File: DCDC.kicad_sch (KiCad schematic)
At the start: 58 parts, among them Q2 TCKE800NL, U16 AP3441SHE-7B, U3 AP64502QSP-13, U5 AP64502, U6 CH221K

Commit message: change cad data
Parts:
- removed C108: 100n, Capacitor_SMD:C_0402_1005Metric, symbol Device:C
- added D12: D, CM5IO:US2H_TOS, symbol Device:D
- added D13: D, CM5IO:SOD-963 CST2C_TOS, symbol Device:D
- C133: renamed from C111; value 4.7nF -> 22pF; footprint Capacitor_SMD:C_0402_1005Metric -> Capacitor_SMD:C_0603_1608Metric_Pad1.08x0.95mm_HandSolder
- C18: renamed from C4; footprint Capacitor_SMD:C_0805_2012Metric_Pad1.18x1.45mm_HandSolder -> Capacitor_SMD:C_1206_3216Metric_Pad1.33x1.80mm_HandSolder
- C19: renamed from C5; footprint Capacitor_SMD:C_0805_2012Metric_Pad1.18x1.45mm_HandSolder -> Capacitor_SMD:C_1206_3216Metric_Pad1.33x1.80mm_HandSolder
- C20: renamed from C6; footprint Capacitor_SMD:C_0805_2012Metric_Pad1.18x1.45mm_HandSolder -> Capacitor_SMD:C_1206_3216Metric_Pad1.33x1.80mm_HandSolder
- C21: renamed from C7; footprint Capacitor_SMD:C_0805_2012Metric_Pad1.18x1.45mm_HandSolder -> Capacitor_SMD:C_1206_3216Metric_Pad1.33x1.80mm_HandSolder
- C28: renamed from C14; footprint Capacitor_SMD:C_0805_2012Metric_Pad1.18x1.45mm_HandSolder -> Capacitor_SMD:C_1206_3216Metric_Pad1.33x1.80mm_HandSolder
- C29: renamed from C15; footprint Capacitor_SMD:C_0805_2012Metric_Pad1.18x1.45mm_HandSolder -> Capacitor_SMD:C_1206_3216Metric_Pad1.33x1.80mm_HandSolder
- C30: renamed from C16; footprint Capacitor_SMD:C_0805_2012Metric_Pad1.18x1.45mm_HandSolder -> Capacitor_SMD:C_1206_3216Metric_Pad1.33x1.80mm_HandSolder
- C31: renamed from C17; footprint Capacitor_SMD:C_0805_2012Metric_Pad1.18x1.45mm_HandSolder -> Capacitor_SMD:C_1206_3216Metric_Pad1.33x1.80mm_HandSolder
- C44: renamed from C30; footprint Capacitor_SMD:C_0805_2012Metric_Pad1.18x1.45mm_HandSolder -> Capacitor_SMD:C_0402_1005Metric_Pad0.74x0.62mm_HandSolder
- R65: renamed from R48; value 10K 1% -> 100kΩ; footprint Resistor_SMD:R_0402_1005Metric -> Resistor_SMD:R_0603_1608Metric_Pad0.98x0.95mm_HandSolder
- R67: renamed from R47; value 2.2K 1% -> 100kΩ; footprint Resistor_SMD:R_0402_1005Metric -> Resistor_SMD:R_0603_1608Metric_Pad0.98x0.95mm_HandSolder
- U17: renamed from U16; value AP3441SHE-7B -> AP3445LW6-7; footprint Package_DFN_QFN:DFN-8-1EP_2x2mm_P0.5mm_EP1.05x1.75mm -> Package_TO_SOT_SMD:SOT-23-6_Handsoldering
- renumbered C91 to C114, C88 to C115, C89 to C116, C90 to C117, C107 to C127, C106 to C130, C3 to C16, C8 to C22, C9 to C23, C10 to C24, C11 to C25, C13 to C27, C18 to C32, C19 to C33, C20 to C34, C21 to C35, C26 to C40, R3 to R13, R4 to R14, R5 to R15, R6 to R16, R10 to R20, R11 to R21, R12 to R22, R13 to R23, R14 to R24, R15 to R25, R16 to R26, R17 to R27, R19 to R28, R49 to R66, R50 to R68, R18 to R69, U3 to U5, U5 to U7, U6 to U8
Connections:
- net 5V: now also U17.1 (EN), U17.4 (VIN); no longer U17.3 (VIN), U17.7 (EN)
- net GND: now also U17.2 (GND), D12.2 (A), D13.2 (A); no longer U17.4 (PGND), U17.8 (SGND), U17.9 (PAD)
- net VBUS: now also D13.1 (K); no longer C23.1, C25.1, C33.1, C35.1, Q2.6 (VOUT), Q2.7 (VOUT_2), Q2.8 (VOUT_3), TP3.1, U5.2 (VIN), U5.3 (EN), U7.2 (VIN), U7.3 (EN)
- net at L4.1: now also U17.3 (LX); no longer U17.6 (LX)
- net FB: no longer names the net of C133.2, R65.2, R67.1
- net FB: now also U17.6 (FB); no longer U17.1 (FB)
- new net +12V: C23.1, C25.1, C33.1, C35.1, D12.1 (K), Q2.6 (VOUT), Q2.7 (VOUT_2), Q2.8 (VOUT_3), TP3.1, U5.2 (VIN), U5.3 (EN), U7.2 (VIN), U7.3 (EN)
- no-connect marks 2 -> 1
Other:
- note added: "1.2V DCDC"
- note added: "3.3V DCDC"
- note added: "5V DCDC"
- moved on the sheet: C114, C115, C116, C117, C127, C130, C133, C40, C44, L4, Q2, R25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

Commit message: remove efuse
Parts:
- removed C44: 1μF, Capacitor_SMD:C_0402_1005Metric_Pad0.74x0.62mm_HandSolder, symbol Device:C
- removed D12: D, CM5IO:US2H_TOS, symbol Device:D
- removed D13: D, CM5IO:SOD-963 CST2C_TOS, symbol Device:D
- removed Q2: TCKE800NL, CM5IO:TCKE800NL, symbol TCKE800NL:TCKE800NL
- removed R25: 36kΩ, Resistor_SMD:R_0603_1608Metric_Pad0.98x0.95mm_HandSolder, symbol Device:R
- removed R28: 1kΩ, Resistor_SMD:R_0603_1608Metric_Pad0.98x0.95mm_HandSolder, symbol Device:R
- removed R69: 10kΩ, Resistor_SMD:R_0603_1608Metric_Pad0.98x0.95mm_HandSolder, symbol Device:R
- removed TP3: TestPoint, TestPoint:TestPoint_Pad_2.0x2.0mm, symbol Connector:TestPoint
- renumbered C16 to C10, C114 to C103, C115 to C104, C116 to C105, C117 to C106, C127 to C114, C130 to C120, C133 to C121, C18 to C14, C19 to C15, C20 to C16, C21 to C17, C22 to C18, C23 to C19, C24 to C20, C25 to C21, C27 to C23, C28 to C24, C29 to C25, C30 to C26, C31 to C27, C32 to C28, C33 to C29, C34 to C30, C35 to C31, C40 to C33, R26 to R25, R27 to R26, R65 to R64, R66 to R65, R67 to R66, R68 to R67, TP4 to TP3, U17 to U18, U8 to U9
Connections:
- net +12V is gone; now on net VBUS: C19.1, C21.1, C29.1, C31.1, U5.2 (VIN), U5.3 (EN), U7.2 (VIN), U7.3 (EN)

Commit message: add sata capacitor
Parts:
- renumbered C103 to C113, C106 to C114, C105 to C115, C104 to C116, C114 to C124, C120 to C130, C121 to C131, C10 to C14, C14 to C18, C15 to C19, C17 to C20, C16 to C21, C18 to C22, C19 to C23, C20 to C24, C21 to C25, C23 to C30, C24 to C32, C25 to C33, C27 to C34, C26 to C35, C28 to C36, C29 to C37, C30 to C38, C31 to C39, C33 to C41, R14 to R13, R13 to R14, R24 to R23, R23 to R24, R64 to R67, R65 to R68, R66 to R69, R67 to R71

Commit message: change design
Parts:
- C24, C38: footprint Capacitor_SMD:C_0603_1608Metric_Pad1.08x0.95mm_HandSolder -> Capacitor_SMD:C_0402_1005Metric_Pad0.74x0.62mm_HandSolder
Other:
- note removed: "eFuse"
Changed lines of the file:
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@@
 		)
 	)
-	(text "eFuse"
-		(exclude_from_sim no)
-		(at 250.7899 125.73 0)
-		(effects
-			(font
-				(size 2.54 2.54)
-			)
-		)
-	)
 	(text "1.2V DCDC\n"
 		(exclude_from_sim no)
@@
 			)
 		)
-		(property "Footprint" "Capacitor_SMD:C_0603_1608Metric_Pad1.08x0.95mm_HandSolder"
+		(property "Footprint" "Capacitor_SMD:C_0402_1005Metric_Pad0.74x0.62mm_HandSolder"
 			(at 113.3348 48.26 0)
 			(effects
@@
 			)
 		)
-		(property "Footprint" "Capacitor_SMD:C_0603_1608Metric_Pad1.08x0.95mm_HandSolder"
+		(property "Footprint" "Capacitor_SMD:C_0402_1005Metric_Pad0.74x0.62mm_HandSolder"
 			(at 112.0648 95.25 0)
 			(effects

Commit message: add logp
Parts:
- renumbered R13 to R10, R14 to R11, R15 to R12, R16 to R13, R20 to R17, R21 to R18, R22 to R19, R23 to R20, R24 to R21, R25 to R22, R26 to R23, R67 to R65, R68 to R66, R69 to R67, R71 to R69
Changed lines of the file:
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@@
 	(label "5V"
 		(at 195.58 36.83 0)
-		(fields_autoplaced yes)
 		(effects
 			(font
@@
 	(label "5V"
 		(at 33.02 143.51 0)
-		(fields_autoplaced yes)
 		(effects
 			(font
@@
 		(shape output)
 		(at 201.93 86.36 0)
-		(fields_autoplaced yes)
 		(effects
 			(font
@@
 		(shape input)
 		(at 24.13 39.37 180)
-		(fields_autoplaced yes)
 		(effects
 			(font
@@
 		(shape input)
 		(at 226.06 27.94 180)
-		(fields_autoplaced yes)
 		(effects
 			(font
@@
 		(shape output)
 		(at 199.39 36.83 0)
-		(fields_autoplaced yes)
 		(effects
 			(font
@@
 		(shape input)
 		(at 224.79 44.45 180)
-		(fields_autoplaced yes)
 		(effects
 			(font
@@
 		(shape input)
 		(at 224.79 41.91 180)
-		(fields_autoplaced yes)
 		(effects
 			(font
@@
 		(shape output)
 		(at 147.32 143.51 0)
-		(fields_autoplaced yes)
 		(effects
 			(font
@@
 		(shape input)
 		(at 25.4 88.9 180)
-		(fields_autoplaced yes)
 		(effects
 			(font
@@
 		(on_board yes)
 		(dnp no)
-		(property "Reference" "R67"
+		(property "Reference" "R65"
 			(at 102.108 146.1516 0)
 			(effects
@@
 			(project "mainboard4"
 				(path "/dd07ab80-a59c-44f4-ac7d-849e21e1384e/eab21d37-4422-449e-812a-90afc228ebcf"
-					(reference "R67")
+					(reference "R65")
 					(unit 1)
 				)
@@
 		(dnp no)
 		(fields_autoplaced yes)
-		(property "Reference" "R13"
+		(property "Reference" "R10"
 			(at 132.08 88.8999 0)
 			(effects
@@
 			(project "mainboard4"
 				(path "/dd07ab80-a59c-44f4-ac7d-849e21e1384e/eab21d37-4422-449e-812a-90afc228ebcf"
-					(reference "R13")
+					(reference "R10")
 					(unit 1)
 				)
@@
 		(dnp no)
 		(fields_autoplaced yes)
-		(property "Reference" "R25"
+		(property "Reference" "R22"
 			(at 236.22 49.53 0)
 			(effects
@@
 			(project "mainboard4"
 				(path "/dd07ab80-a59c-44f4-ac7d-849e21e1384e/eab21d37-4422-449e-812a-90afc228ebcf"
-					(reference "R25")
+					(reference "R22")
 					(unit 1)
 				)
@@
 		(dnp no)
 		(fields_autoplaced yes)
-		(property "Reference" "R16"
+		(property "Reference" "R13"
 			(at 82.55 96.5199 0)
 			(effects
@@
 			(project "mainboard4"
 				(path "/dd07ab80-a59c-44f4-ac7d-849e21e1384e/eab21d37-4422-449e-812a-90afc228ebcf"
-					(reference "R16")
+					(reference "R13")
 					(unit 1)
 				)
@@
 		(dnp no)
 		(fields_autoplaced yes)
-		(property "Reference" "R22"
+		(property "Reference" "R19"
 			(at 82.55 46.9899 0)
 			(effects
@@
 			(project ""
 				(path "/dd07ab80-a59c-44f4-ac7d-849e21e1384e/eab21d37-4422-449e-812a-90afc228ebcf"
-					(reference "R22")
+					(reference "R19")
 					(unit 1)
 				)
@@
 		(on_board yes)
 		(dnp no)
-		(property "Reference" "R24"
+		(property "Reference" "R21"
 			(at 232.664 22.352 90)
 			(effects
@@
 			(project "mainboard4"
 				(path "/dd07ab80-a59c-44f4-ac7d-849e21e1384e/eab21d37-4422-449e-812a-90afc228ebcf"
-					(reference "R24")
+					(reference "R21")
 					(unit 1)
 				)
@@
 		(dnp no)
 		(fields_autoplaced yes)
-		(property "Reference" "R21"
+		(property "Reference" "R18"
 			(at 82.55 54.6099 0)
 			(effects
@@
 			(project "mainboard4"
 				(path "/dd07ab80-a59c-44f4-ac7d-849e21e1384e/eab21d37-4422-449e-812a-90afc228ebcf"
-					(reference "R21")
+					(reference "R18")
 					(unit 1)
 				)
@@
 		(dnp no)
 		(fields_autoplaced yes)
-		(property "Reference" "R26"
+		(property "Reference" "R23"
 			(at 246.38 49.53 0)
 			(effects
@@
 			(project "mainboard4"
 				(path "/dd07ab80-a59c-44f4-ac7d-849e21e1384e/eab21d37-4422-449e-812a-90afc228ebcf"
-					(reference "R26")
+					(reference "R23")
 					(unit 1)
 				)
@@
 		(dnp no)
 		(fields_autoplaced yes)
-		(property "Reference" "R71"
+		(property "Reference" "R69"
 			(at 134.62 46.9899 0)
 			(effects
@@
 			(project "mainboard4"
 				(path "/dd07ab80-a59c-44f4-ac7d-849e21e1384e/eab21d37-4422-449e-812a-90afc228ebcf"
-					(reference "R71")
+					(reference "R69")
 					(unit 1)
 				)
@@
 		(dnp no)
 		(fields_autoplaced yes)
-		(property "Reference" "R68"
+		(property "Reference" "R66"
 			(at 134.62 39.3699 0)
 			(effects
@@
 			(project "mainboard4"
 				(path "/dd07ab80-a59c-44f4-ac7d-849e21e1384e/eab21d37-4422-449e-812a-90afc228ebcf"
-					(reference "R68")
+					(reference "R66")
 					(unit 1)
 				)
@@
 		(on_board yes)
 		(dnp no)
-		(property "Reference" "R23"
+		(property "Reference" "R20"
 			(at 251.714 20.32 90)
 			(effects
@@
 			(project "mainboard4"
 				(path "/dd07ab80-a59c-44f4-ac7d-849e21e1384e/eab21d37-4422-449e-812a-90afc228ebcf"
-					(reference "R23")
+					(reference "R20")
 					(unit 1)
 				)
@@
 		(on_board yes)
 		(dnp no)
-		(property "Reference" "R69"
+		(property "Reference" "R67"
 			(at 102.108 155.0416 0)
 			(effects
@@
 			(project "mainboard4"
 				(path "/dd07ab80-a59c-44f4-ac7d-849e21e1384e/eab21d37-4422-449e-812a-90afc228ebcf"
-					(reference "R69")
+					(reference "R67")
 					(unit 1)
 				)
@@
 		(dnp no)
 		(fields_autoplaced yes)
-		(property "Reference" "R20"
+		(property "Reference" "R17"
 			(at 134.62 54.6099 0)
 			(effects
@@
 			(project "mainboard4"
 				(path "/dd07ab80-a59c-44f4-ac7d-849e21e1384e/eab21d37-4422-449e-812a-90afc228ebcf"
-					(reference "R20")
+					(reference "R17")
 					(unit 1)
 				)
@@
 		(dnp no)
 		(fields_autoplaced yes)
-		(property "Reference" "R15"
+		(property "Reference" "R12"
 			(at 82.55 104.1399 0)
 			(effects
@@
 			(project "mainboard4"
 				(path "/dd07ab80-a59c-44f4-ac7d-849e21e1384e/eab21d37-4422-449e-812a-90afc228ebcf"
-					(reference "R15")
+					(reference "R12")
 					(unit 1)
 				)
@@
 		(dnp no)
 		(fields_autoplaced yes)
-		(property "Reference" "R14"
+		(property "Reference" "R11"
 			(at 132.08 100.3299 0)
 			(effects
@@
 			(project "mainboard4"
 				(path "/dd07ab80-a59c-44f4-ac7d-849e21e1384e/eab21d37-4422-449e-812a-90afc228ebcf"
-					(reference "R14")
+					(reference "R11")
 					(unit 1)
 				)

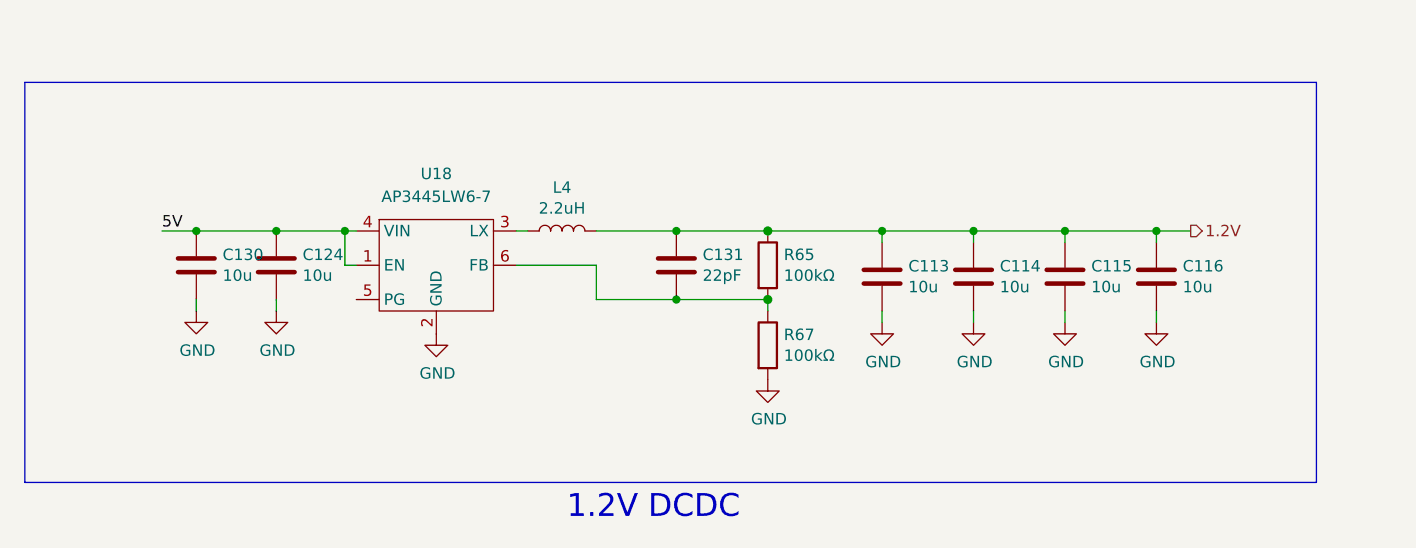
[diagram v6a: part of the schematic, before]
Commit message: delete usb hub
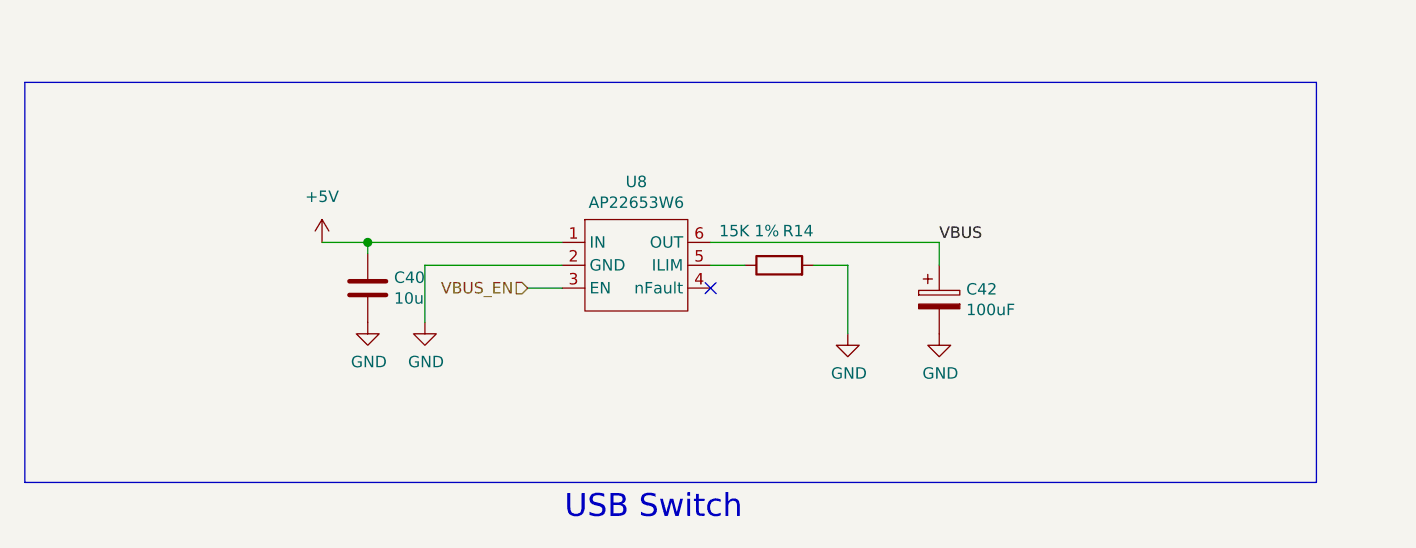
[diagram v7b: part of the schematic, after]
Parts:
- removed C113, C114, C115, C116, C124, C130: 10u, Capacitor_SMD:C_0805_2012Metric, symbol Device:C
- removed C131: 22pF, Capacitor_SMD:C_0603_1608Metric_Pad1.08x0.95mm_HandSolder, symbol Device:C
- removed L4: 2.2uH, Inductor_SMD:L_1210_3225Metric_Pad1.42x2.65mm_HandSolder, symbol Device:L
- removed R65, R67: 100kΩ, Resistor_SMD:R_0603_1608Metric_Pad0.98x0.95mm_HandSolder, symbol Device:R
- removed U18: AP3445LW6-7, Package_TO_SOT_SMD:SOT-23-6_Handsoldering, symbol CM5IO:AP3441SHE-7B
- added C40: 10u, Capacitor_SMD:C_0805_2012Metric, symbol Device:C
- added C42: 100uF, Capacitor_Tantalum_SMD:CP_EIA-7343-31_Kemet-D, symbol Device:C_Polarized
- added R14: 15K 1%, Resistor_SMD:R_0603_1608Metric_Pad0.98x0.95mm_HandSolder, symbol Device:R
- added U8: AP22653W6, Package_TO_SOT_SMD:SOT-23-6, symbol CM5IO:AP2553W6
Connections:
- net GND: now also C40.2, C42.2, R14.2, U8.2 (GND)
- net VBUS: now also C42.1, U8.6 (OUT)
- new net: R14.1, U8.5 (ILIM)
- new net +5V: C40.1, U8.1 (IN)
- new net VBUS_EN: U8.3 (EN)
- no-connect marks 1 -> 2
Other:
- note added: "USB Switch"
- note removed: "1.2V DCDC"
